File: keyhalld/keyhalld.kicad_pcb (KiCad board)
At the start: 4 copper layers, 96 parts, among them J1 Conn_ARM_SWD_TagConnect_TC203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, J2 USB_C_Receptacle_USB2.0_16P, J3 Conn_01x05_Pin, SW1 HallSwitch, SW10 HallSwitch, SW11 HallSwitch, SW12 HallSwitch, SW13 HallSwitch, SW14 HallSwitch, SW15 HallSwitch, SW16 HallSwitch, SW17 HallSwitch, SW18 HallSwitch, SW2 HallSwitch, SW3 HallSwitch, SW4 HallSwitch, SW5 HallSwitch, SW6 HallSwitch, SW7 HallSwitch, SW8 HallSwitch, SW9 HallSwitch, U1 AMS1117-3.3, U10 DRV5055A4xDBZxQ1, U11 DRV5055A4xDBZxQ1, U12 DRV5055A4xDBZxQ1, U13 DRV5055A4xDBZxQ1, U14 DRV5055A4xDBZxQ1, U15 DRV5055A4xDBZxQ1, U16 DRV5055A4xDBZxQ1, U17 DRV5055A4xDBZxQ1, U18 DRV5055A4xDBZxQ1, U19 DRV5055A4xDBZxQ1, U2 USBLC6-2SC6, U20 DRV5055A4xDBZxQ1, U21 DRV5055A4xDBZxQ1, U22 DRV5055A4xDBZxQ1, U3 RP2350A, U4 CD74HC4067M, U5 DRV5055A4xDBZxQ1, U6 DRV5055A4xDBZxQ1, U7 DRV5055A4xDBZxQ1, U8 DRV5055A4xDBZxQ1, U9 DRV5055A4xDBZxQ1, Y1 12MHz

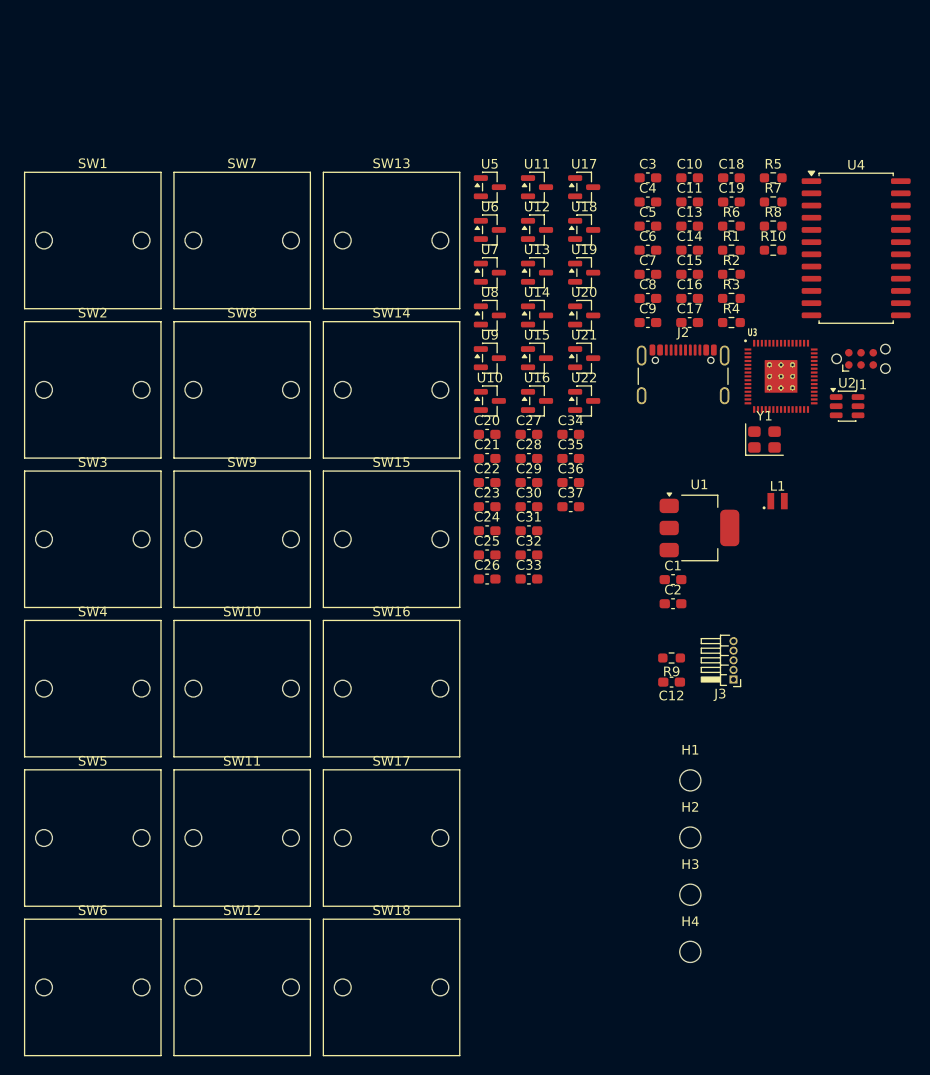
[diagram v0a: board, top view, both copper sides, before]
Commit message: move common libs to root; add fp to ldo
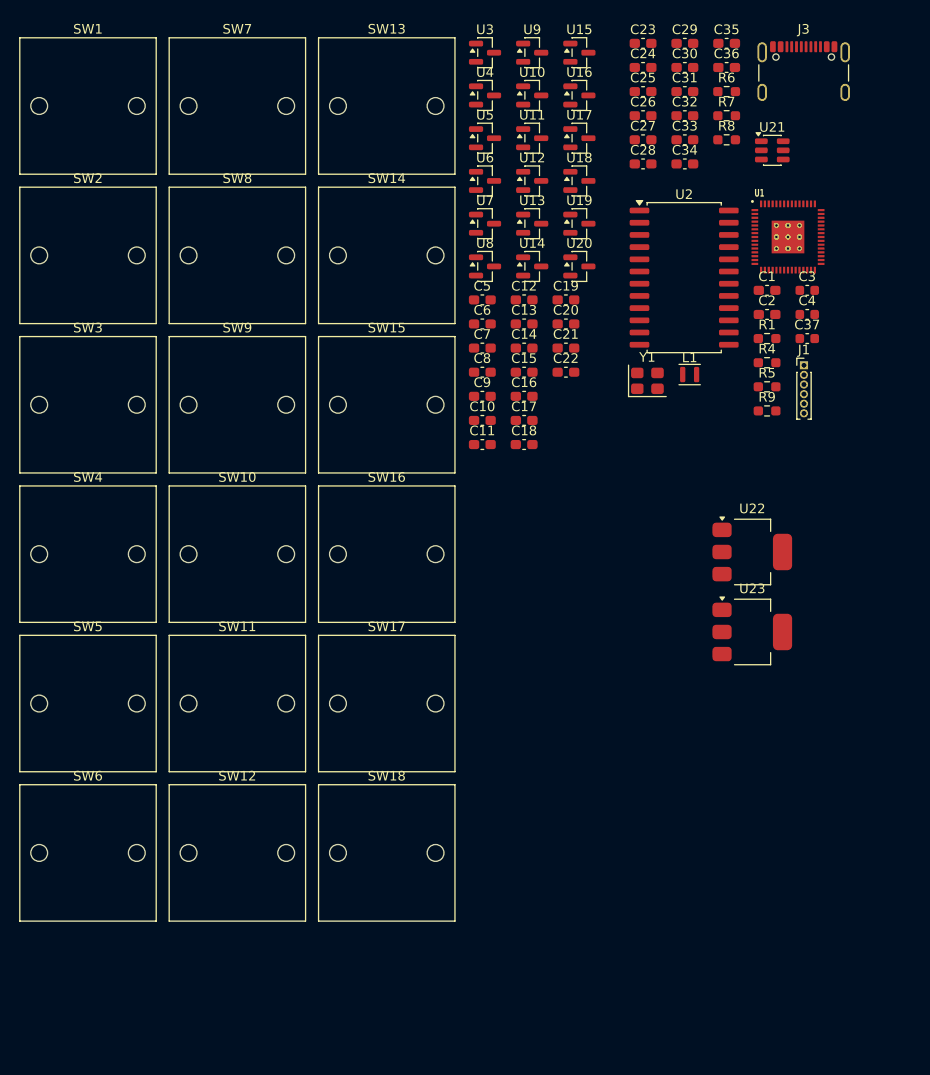
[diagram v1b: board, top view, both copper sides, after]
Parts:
- removed H1, H2, H3, H4: MountingHole_Pad, MountingHole:MountingHole_2.2mm_M2
- removed J2: USB_C_Receptacle_USB2.0_16P, Connector_USB:USB_C_Receptacle_GCT_USB4105-xx-A_16P_TopMnt_Horizontal
- removed R10: 33R, Resistor_SMD:R_0603_1608Metric_Pad0.98x0.95mm_HandSolder
- removed R2: 5K1, Resistor_SMD:R_0603_1608Metric_Pad0.98x0.95mm_HandSolder
- removed R3: 1.5K, Resistor_SMD:R_0603_1608Metric_Pad0.98x0.95mm_HandSolder
- added U23: TLV1117-33, Package_TO_SOT_SMD:SOT-223, F.Cu at (115.4, 89.5)
- C1: value 47u -> 15p
- C10, C11, C12, C15, C17, C18, C19, C5, C6, C7, C8, C9: value 100n -> 10n
- C13, C14, C16: value 4.7u -> 10n
- C2: value 22u -> 15p
- C23, C24, C25, C26, C27, C28, C29, C30, C33, C34: value 10n -> 100n
- C3, C4: value 15p -> 4.7u; footprint Capacitor_SMD:C_0603_1608Metric_Pad1.08x0.95mm_HandSolder -> Capacitor_SMD:C_0603_1608Metric
- C31, C32, C35, C36: value 10n -> 1u
- C37: value 10n -> 4.7u; footprint Capacitor_SMD:C_0603_1608Metric_Pad1.08x0.95mm_HandSolder -> Capacitor_SMD:C_0603_1608Metric
- J1: value Conn_ARM_SWD_TagConnect_TC2030-NL -> Conn_01x06_Pin; footprint Connector:Tag-Connect_TC2030-IDC-NL_2x03_P1.27mm_Vertical -> Connector_PinHeader_1.00mm:PinHeader_1x06_P1.00mm_Vertical
- J3: value Conn_01x05_Pin -> USB_C_Receptacle_USB2.0_16P; footprint Connector_PinHeader_1.00mm:PinHeader_1x05_P1.00mm_Horizontal -> Connector_USB:USB_C_Receptacle_GCT_USB4105-xx-A_16P_TopMnt_Horizontal
- L1: value 3.3u -> 3.3uH; footprint RPI:abracon_aota-b201610s3r3-101-t -> Inductor_SMD:L_Murata_DFE201610P
- R1: value 5K1 -> 1K
- R4, R5: value 1.5K -> 22R
- R6: value 1K -> 5K1
- R7: value 22R -> 5K1
- R8: value 22R -> 1.5K
- R9: value 1.5K -> 33
- SW1, SW10, SW11, SW12, SW13, SW14, SW15, SW16, SW17, SW18, SW2, SW3, SW4, SW5, SW6, SW7, SW8, SW9: footprint Custom:Custom_MX_PCB_1.00u -> Library:Custom_MX_PCB_1.00u
- U1: value AMS1117-3.3 -> RP2350A; footprint Package_TO_SOT_SMD:SOT-223-3_TabPin2 -> RPI:rpi_rp2350a_vias
- U2: value USBLC6-2SC6 -> CD74HC4067M; footprint Package_TO_SOT_SMD:SOT-23-6 -> Package_SO:SOIC-24W_7.5x15.4mm_P1.27mm
- U21: value DRV5055A4xDBZxQ1 -> USBLC6-2SC6; footprint Package_TO_SOT_SMD:SOT-23 -> Package_TO_SOT_SMD:SOT-23-6
- U22: value DRV5055A4xDBZxQ1 -> TLV1117-33; footprint Package_TO_SOT_SMD:SOT-23 -> Package_TO_SOT_SMD:SOT-223
- U3: value RP2350A -> DRV5055A4xDBZxQ1; footprint RPI:rpi_rp2350a_vias -> Package_TO_SOT_SMD:SOT-23
- U4: value CD74HC4067M -> DRV5055A4xDBZxQ1; footprint Package_SO:SOIC-24W_7.5x15.4mm_P1.27mm -> Package_TO_SOT_SMD:SOT-23
- moved J3 62.6 mm to (120.8, 32.3), turned to 0 degrees
- moved C23 50.9 mm to (104.1, 28.3)
- moved C24 50.9 mm to (104.1, 30.8)
- moved C26 50.9 mm to (104.1, 35.8)
- moved C25 50.9 mm to (104.1, 33.3)
- moved C31 48.5 mm to (108.4, 33.3)
- moved C29 48.5 mm to (108.4, 28.3)
- moved C30 48.5 mm to (108.4, 30.8)
- moved C32 48.5 mm to (108.4, 35.8)
- moved C33 48.5 mm to (108.4, 38.3)
- moved C35 46.2 mm to (112.8, 28.3)
- moved C36 46.2 mm to (112.8, 30.8)
- moved U3 45.7 mm to (87.6, 29.2)
- moved C12 42.6 mm to (91.7, 55.0), turned to 0 degrees
- moved U4 41.8 mm to (87.6, 33.7)
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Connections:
- C1 pad 1: +5V -> GND
- C1 pad 2: GND -> XIN
- C10 pad 1: +3.3V -> GND
- C10 pad 2: GND -> +3.3VA
- C11 pad 1: +3.3V -> GND
- C11 pad 2: GND -> +3.3VA
- C12 pad 2: RUN -> +3.3VA
- C13 pad 1: +1V1 -> GND
- C13 pad 2: GND -> +3.3VA
- C14 pad 1: +3.3V -> GND
- C14 pad 2: GND -> +3.3VA
- C15 pad 1: +1V1 -> GND
- C15 pad 2: GND -> +3.3VA
- C16 pad 1: +3.3VA -> GND
- C16 pad 2: GND -> +3.3VA
- C17 pad 1: +1V1 -> GND
- C17 pad 2: GND -> +3.3VA
- C18 pad 1: +3.3VA -> GND
- C18 pad 2: GND -> +3.3VA
- C19 pad 1: +1V1 -> GND
- C19 pad 2: GND -> +3.3VA
- C2 pad 1: +3.3V -> GND
- C2 pad 2: GND -> Net-(C2-Pad2)
- C23 pad 1: GND -> +3.3V
- C23 pad 2: +3.3VA -> GND
- C24 pad 1: GND -> +3.3V
- C24 pad 2: +3.3VA -> GND
- C25 pad 1: GND -> +3.3V
- C25 pad 2: +3.3VA -> GND
- C26 pad 1: GND -> +3.3V
- C26 pad 2: +3.3VA -> GND
- C27 pad 1: GND -> +3.3V
- C27 pad 2: +3.3VA -> GND
- C28 pad 1: GND -> +3.3V
- C28 pad 2: +3.3VA -> GND
- C29 pad 1: GND -> +3.3V
- C29 pad 2: +3.3VA -> GND
- C3 pad 1: GND -> +1V1
- C3 pad 2: XIN -> GND
- C30 pad 1: GND -> +1V1
- C30 pad 2: +3.3VA -> GND
- C31 pad 1: GND -> +5V
- C31 pad 2: +3.3VA -> GND
- C32 pad 1: GND -> +5V
- C32 pad 2: +3.3VA -> GND
- C33 pad 1: GND -> +1V1
- C33 pad 2: +3.3VA -> GND
- C34 pad 1: GND -> +1V1
- C34 pad 2: +3.3VA -> GND
- C35 pad 1: GND -> +3.3V
- C35 pad 2: +3.3VA -> GND
- C36 pad 1: GND -> +3.3VA
- C36 pad 2: +3.3VA -> GND
- C37 pad 1: GND -> Net-(U1-VREG_AVDD)
- C37 pad 2: +3.3VA -> GND
- C4 pad 1: GND -> +3.3V
- C4 pad 2: Net-(C4-Pad2) -> GND
- C5 pad 1: +3.3V -> GND
- C5 pad 2: GND -> +3.3VA
- C6 pad 1: +3.3V -> GND
- C6 pad 2: GND -> +3.3VA
- C7 pad 1: +3.3V -> GND
- C7 pad 2: GND -> +3.3VA
- C8 pad 1: +3.3V -> GND
- C8 pad 2: GND -> +3.3VA
- C9 pad 1: +3.3V -> GND
- C9 pad 2: GND -> +3.3VA
- J1 pad 2: SWDIO -> SWCLK
- J1 pad 3: RUN -> SWDIO
- J1 pad 4: SWCLK -> RUN
- J1 pad 5: GND -> DBG_TX
- J1 pad 6: unconnected-(J1-SWO-Pad6) -> GND
- L1 pad 2: Net-(U3-VREG_LX) -> Net-(U1-VREG_LX)
- R1 pad 1: Net-(J2-CC1) -> XOUT
- R1 pad 2: GND -> Net-(C2-Pad2)
- R4 pad 1: I2C_SDA -> Net-(U1-USB_DP)
- R4 pad 2: +3.3V -> D+
- R5 pad 1: I2C_SCK -> D-
- R5 pad 2: +3.3V -> Net-(U1-USB_DM)
- R6 pad 1: XOUT -> Net-(J3-CC1)
- R6 pad 2: Net-(C4-Pad2) -> GND
- R7 pad 1: Net-(U3-USB_DP) -> GND
- R7 pad 2: D+ -> Net-(J3-CC2)
- R8 pad 1: D- -> /USB & Power/CONN_D+
- R8 pad 2: Net-(U3-USB_DM) -> +3.3V
- R9 pad 1: RUN -> Net-(U1-VREG_AVDD)
- R9 pad 2: +3.3V -> +3.3VA
- U1 pad 1: GND -> +3.3V
- U1 pad 2: +3.3V -> DBG_TX
- U1 pad 3: +5V -> unconnected-(U1-GPIO1-Pad3)
- U10 pad 2: A1 -> AM10
- U11 pad 2: AM2 -> AM3
- U12 pad 2: AM10 -> AM11
- U13 pad 2: AM3 -> AM4
- U14 pad 2: AM11 -> AM12
- U15 pad 2: AM4 -> AM5
- U16 pad 2: AM12 -> AM13
- U17 pad 2: AM5 -> AM6
- U18 pad 2: AM13 -> AM14
- U19 pad 2: AM6 -> AM7
- U2 pad 1: /CONN_D- -> Net-(U1-GPIO28_ADC2)
- U2 pad 2: GND -> AM7
- U2 pad 3: /CONN_D+ -> AM6
- U2 pad 4: D+ -> AM5
- U2 pad 5: +5V -> AM4
- U2 pad 6: D- -> AM3
- U20 pad 2: AM14 -> AM15
- U21 pad 1: +3.3VA -> /USB & Power/CONN_D-
- U21 pad 2: AM7 -> GND
- U21 pad 3: GND -> /USB & Power/CONN_D+
- U22 pad 1: +3.3VA -> GND
- U22 pad 2: AM15 -> +3.3V
- U22 pad 3: GND -> +5V
- U3 pad 1: +3.3V -> +3.3VA
- U3 pad 2: I2C_SDA -> AM0
- U3 pad 3: I2C_SCK -> GND
- U4 pad 1: Net-(U3-GPIO28_ADC2) -> +3.3VA
- U4 pad 2: AM7 -> AM8
- U4 pad 3: AM6 -> GND
- U5 pad 2: AM0 -> A0
- U6 pad 2: AM8 -> AM1
- U7 pad 2: A0 -> AM9
- U8 pad 2: AM1 -> A1
- U9 pad 2: AM9 -> AM2
- Y1 pad 3: Net-(C4-Pad2) -> Net-(C2-Pad2)

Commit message: Started PCB Implementation
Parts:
- removed R9: 33, Resistor_SMD:R_0603_1608Metric_Pad0.98x0.95mm_HandSolder
- added C38: 1u, Capacitor_SMD:C_0603_1608Metric_Pad1.08x0.95mm_HandSolder, F.Cu at (-115.4, 142.5)
- added D1: WS2812B-2020, LED_SMD:LED_WS2812B-2020_PLCC4_2.0x2.0mm, F.Cu at (155.9, 46.5)
- added H1: MP, MountingHole:MountingHole_3.2mm_M3_Pad, F.Cu at (151.0, 61.0)
- added H2: MP, MountingHole:MountingHole_3.2mm_M3_Pad, F.Cu at (385.0, 61.0)
- added H3: MP, MountingHole:MountingHole_3.2mm_M3_Pad, F.Cu at (385.0, 119.0)
- added H4: MP, MountingHole:MountingHole_3.2mm_M3_Pad, F.Cu at (151.0, 120.0)
- added H5: MP, MountingHole:MountingHole_3.2mm_M3_Pad, F.Cu at (242.0, 72.0)
- added H6: MP, MountingHole:MountingHole_3.2mm_M3_Pad, F.Cu at (314.0, 72.0)
- added H7: MP, MountingHole:MountingHole_3.2mm_M3_Pad, F.Cu at (314.0, 119.0)
- added H8: MP, MountingHole:MountingHole_3.2mm_M3_Pad, F.Cu at (242.0, 119.0)
- added J2: Conn_01x04_Pin, Connector_PinHeader_2.54mm:PinHeader_1x04_P2.54mm_Vertical, F.Cu at (148.0, 92.4)
- added R2: 22R, Resistor_SMD:R_0603_1608Metric_Pad0.98x0.95mm_HandSolder, F.Cu at (162.8, 81.3)
- added R3: 22R, Resistor_SMD:R_0603_1608Metric_Pad0.98x0.95mm_HandSolder, F.Cu at (164.5, 81.3)
- added SW19: HallSwitch, Library:Custom_MX_PCB_1.00u, F.Cu at (359.1, 91.0)
- added SW20: HallSwitch, Library:Custom_MX_PCB_1.00u, F.Cu at (377.1, 91.0)
- C1, C2: value 15p -> 4.7u; footprint Capacitor_SMD:C_0603_1608Metric_Pad1.08x0.95mm_HandSolder -> Capacitor_SMD:C_0603_1608Metric
- C23, C24: value 100n -> 10n
- C31, C32: value 1u -> 100n
- C37: value 4.7u -> 1u; footprint Capacitor_SMD:C_0603_1608Metric -> Capacitor_SMD:C_0603_1608Metric_Pad1.08x0.95mm_HandSolder
- C4: value 4.7u -> 15p; footprint Capacitor_SMD:C_0603_1608Metric -> Capacitor_SMD:C_0603_1608Metric_Pad1.08x0.95mm_HandSolder
- C5: value 10n -> 15p
- C6: value 10n -> 100n
- J1: footprint Connector_PinHeader_1.00mm:PinHeader_1x06_P1.00mm_Vertical -> Connector_PinHeader_2.54mm:PinHeader_1x06_P2.54mm_Horizontal
- R1: value 1K -> 33
- R4: value 22R -> 1K
- R5: value 22R -> 4.7k
- SW1: value HallSwitch -> RESET; footprint Library:Custom_MX_PCB_1.00u -> Button_Switch_SMD:SW_Tactile_SPST_NO_Straight_CK_PTS636Sx25SMTRLFS
- SW2: value HallSwitch -> USB_BOOT; footprint Library:Custom_MX_PCB_1.00u -> Button_Switch_SMD:SW_Tactile_SPST_NO_Straight_CK_PTS636Sx25SMTRLFS
- U21: value USBLC6-2SC6 -> TLV1117-33; footprint Package_TO_SOT_SMD:SOT-23-6 -> Package_TO_SOT_SMD:SOT-223
- U22: value TLV1117-33 -> USBLC6-2SC6; footprint Package_TO_SOT_SMD:SOT-223 -> Package_TO_SOT_SMD:SOT-23-6
- moved U20 282.5 mm to (377.1, 91.0), turned to 90 degrees
- moved C24 277.3 mm to (375.6, 87.0), turned to 180 degrees
- moved SW18 275.7 mm to (350.1, 72.0)
- moved U19 265.3 mm to (359.1, 91.0), turned to 90 degrees
- moved SW17 263.8 mm to (341.1, 91.0)
- moved C30 262.5 mm to (-124.1, 152.6)
- moved C29 262.5 mm to (-124.1, 150.0)
- moved C23 260.6 mm to (357.9, 87.5), turned to 180 degrees
- moved C35 260.2 mm to (-119.7, 145.0)
- moved C37 256.6 mm to (-119.7, 147.5)
- moved SW16 254.9 mm to (332.1, 72.0)
- moved U18 254.4 mm to (350.1, 72.0), turned to 90 degrees
- moved C33 254.0 mm to (-119.7, 150.0)
- moved C34 254.0 mm to (-119.7, 152.6)
- moved R6 254.0 mm to (-115.4, 145.0)
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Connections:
- C1 pad 1: GND -> +1V1
- C1 pad 2: XIN -> GND
- C2 pad 1: GND -> +3.3V
- C2 pad 2: Net-(C2-Pad2) -> GND
- C23 pad 1: +3.3V -> GND
- C23 pad 2: GND -> +3.3VA
- C24 pad 1: +3.3V -> GND
- C24 pad 2: GND -> +3.3VA
- C3 pad 1: +1V1 -> Net-(U1-VREG_AVDD)
- C30 pad 1: +1V1 -> +3.3V
- C31 pad 1: +5V -> +3.3V
- C32 pad 1: +5V -> +1V1
- C35 pad 1: +3.3V -> +5V
- C36 pad 1: +3.3VA -> +3.3V
- C37 pad 1: Net-(U1-VREG_AVDD) -> +5V
- C4 pad 1: +3.3V -> GND
- C4 pad 2: GND -> XIN
- C5 pad 2: +3.3VA -> Net-(C5-Pad2)
- C6 pad 1: GND -> +5V
- C6 pad 2: +3.3VA -> GND
- R1 pad 1: XOUT -> Net-(U1-VREG_AVDD)
- R1 pad 2: Net-(C2-Pad2) -> +3.3VA
- R4 pad 1: Net-(U1-USB_DP) -> XOUT
- R4 pad 2: D+ -> Net-(C5-Pad2)
- R5 pad 1: D- -> Net-(R5-Pad1)
- R5 pad 2: Net-(U1-USB_DM) -> USB_BOOT
- U1 pad 10: unconnected-(U1-GPIO7-Pad10) -> WS2812_TX
- U1 pad 16: unconnected-(U1-GPIO12-Pad16) -> DBG_TX
- U1 pad 2: DBG_TX -> unconnected-(U1-GPIO0-Pad2)
- U1 pad 59: unconnected-(U1-QSPI_SD1-Pad59) -> GND
- U1 pad 60: unconnected-(U1-QSPI_~{SS}-Pad60) -> USB_BOOT
- U1 pad 7: unconnected-(U1-GPIO4-Pad7) -> MAG_UART_TX
- U1 pad 8: unconnected-(U1-GPIO5-Pad8) -> MAG_UART_RX
- U10 pad 2: AM10 -> AM5
- U11 pad 2: AM3 -> AM6
- U12 pad 2: AM11 -> AM7
- U13 pad 2: AM4 -> AM8
- U14 pad 2: AM12 -> AM9
- U15 pad 2: AM5 -> AM10
- U16 pad 2: AM13 -> AM11
- U17 pad 2: AM6 -> AM12
- U18 pad 2: AM14 -> AM13
- U19 pad 2: AM7 -> AM14
- U21 pad 1: /USB & Power/CONN_D- -> GND
- U21 pad 2: GND -> +3.3V
- U21 pad 3: /USB & Power/CONN_D+ -> +5V
- U21 pad 4: D+ -> (no net)
- U22 pad 1: GND -> /USB & Power/CONN_D-
- U22 pad 2: +3.3V -> GND
- U22 pad 3: +5V -> /USB & Power/CONN_D+
- U22 pad 4: (no net) -> D+
- U3 pad 2: AM0 -> A0
- U4 pad 2: AM8 -> A1
- U5 pad 2: A0 -> AM0
- U7 pad 2: AM9 -> AM2
- U8 pad 2: A1 -> AM3
- U9 pad 2: AM2 -> AM4
- Y1 pad 3: Net-(C2-Pad2) -> Net-(C5-Pad2)
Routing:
- net AM15: track 0.00 -> 108.1 mm
- net +3.3VA: track 0.00 -> 95.6 mm, vias 0 -> 1
- net AM13: track 0.00 -> 95.0 mm
- net AM14: track 0.00 -> 90.8 mm
- net GND: track 0.00 -> 83.8 mm, vias 0 -> 4
- net AM1: track 0.00 -> 81.3 mm
- net AM11: track 0.00 -> 77.1 mm
- net AM12: track 0.00 -> 70.0 mm
- net AM0: track 0.00 -> 66.5 mm
- net AM2: track 0.00 -> 58.0 mm
- net AM10: track 0.00 -> 50.4 mm
- net AM4: track 0.00 -> 46.1 mm
- net AM8: track 0.00 -> 43.7 mm
- net AM6: track 0.00 -> 43.5 mm
- net AM3: track 0.00 -> 39.4 mm
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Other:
- board outline added: 248 x 71 mm

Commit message: Store WIP results
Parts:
- moved SW20 15.4 mm to (392.5, 91.0)
- moved C24 15.4 mm to (391.0, 87.0)
- moved U20 15.4 mm to (392.5, 91.0)
- moved SW19 13.9 mm to (373.0, 91.0)
- moved C23 13.9 mm to (371.8, 87.5)
- moved U19 13.9 mm to (373.0, 91.0)
- moved H2 13.5 mm to (398.5, 61.0)
- moved SW18 13.2 mm to (363.2, 71.0)
- moved C22 13.2 mm to (362.0, 67.5)
- moved U18 13.2 mm to (363.2, 71.0)
- moved H3 13.0 mm to (398.0, 118.0)
- moved SW17 12.4 mm to (353.5, 91.0)
- moved C21 12.4 mm to (352.4, 87.5)
- moved U17 12.4 mm to (353.5, 91.0)
- moved SW16 11.7 mm to (343.8, 71.0)
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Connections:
- J1 pad 2: SWCLK -> SWDIO
- J1 pad 3: SWDIO -> SWCLK
- U1 pad 40: A0 -> Net-(U1-GPIO26_ADC0)
- U1 pad 41: A1 -> A0
- U1 pad 42: Net-(U1-GPIO28_ADC2) -> A1
- U2 pad 1: Net-(U1-GPIO28_ADC2) -> Net-(U1-GPIO26_ADC0)
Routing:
- net AM13: track 95.0 -> 103.3 mm
- net RUN: track 27.5 -> 20.7 mm
- net AM15: track 108.1 -> 114.7 mm
- net AM0: track 66.5 -> 72.7 mm
- net SWDIO: track 31.0 -> 25.2 mm
- net AM2: track 58.0 -> 52.8 mm
- net AM11: track 77.1 -> 81.9 mm
- net +3.3V: track 5.91 -> 2.04 mm, vias 1 -> 0
- net AM14: track 90.8 -> 94.6 mm
- net AM12: track 70.0 -> 73.8 mm
- net AM3: track 39.4 -> 36.0 mm
- net AM10: track 50.4 -> 53.3 mm
- net AM5: track 23.3 -> 20.8 mm
- net +3.3VA: track 95.6 -> 93.2 mm, vias 1 -> 0
- net AM8: track 43.7 -> 41.9 mm
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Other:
- board size 248 x 71 mm -> 261 x 71 mm

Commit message: Almost done with power domain tracing
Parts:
- moved R8 308.6 mm to (183.3, 72.6)
- moved C27 303.8 mm to (174.6, 89.8)
- moved C26 302.7 mm to (175.5, 99.0), turned to -90 degrees
- moved C32 300.8 mm to (177.6, 97.2), turned to -90 degrees
- moved C25 300.4 mm to (173.5, 99.0), turned to -90 degrees
- moved C38 294.5 mm to (174.6, 91.2)
- moved C36 293.1 mm to (174.4, 96.2)
- moved C30 291.3 mm to (161.0, 92.6), turned to 180 degrees
- moved C29 290.4 mm to (161.0, 95.0), turned to 180 degrees
- moved C28 289.6 mm to (161.0, 96.6), turned to 180 degrees
- moved C34 288.1 mm to (161.0, 87.8), turned to 180 degrees
- moved C33 288.1 mm to (163.8, 99.2), turned to 180 degrees
- moved C31 285.0 mm to (161.0, 91.0), turned to 180 degrees
- moved C35 254.4 mm to (129.9, 96.0)
- moved C37 254.4 mm to (129.9, 98.5)
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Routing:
- net +3.3V: track 2.04 -> 38.5 mm, vias 0 -> 3
- net GND: track 83.5 -> 107.6 mm, vias 4 -> 5
- net SWCLK: track 26.2 -> 5.24 mm
- net SWDIO: track 25.2 -> 5.20 mm
- net DBG_TX: track 24.3 -> 4.29 mm, vias 0 -> 1
- net RUN: track 20.7 -> 6.83 mm
- net +1V1: track 12.9 -> 22.3 mm, vias 2 -> 6
- net Net-(C5-Pad2): track 10.8 -> 7.56 mm
- net +3.3VA: track 93.2 -> 96.2 mm
- net XOUT: track 5.65 -> 7.82 mm
- net Net-(U1-USB_DP): track 6.29 -> 5.33 mm
- net USB_BOOT: track 3.66 -> 2.94 mm
- net Net-(U1-VREG_LX): track 6.68 -> 6.14 mm
